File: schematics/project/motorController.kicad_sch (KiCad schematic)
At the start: 0 parts

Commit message: some progress, dust slowly clears
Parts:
- added Q1, Q2, Q3, Q4, Q5, Q6: BSS123, Package_TO_SOT_SMD:SOT-23, symbol Transistor_FET:BSS123
- added R10, R11, R12, R7, R8, R9: 1k, Resistor_SMD:R_0603_1608Metric, symbol Device:R
- added R4, R5, R6: R, Resistor_SMD:R_0603_1608Metric, symbol Device:R
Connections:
- net cruise: now also R10.2
- net hiPoBreak: now also R12.2
- net lowPoBreak: now also R11.2
- net reverse: now also R7.2
- net speed_fast: now also R8.2
- net speed_slow: now also R9.2
- new net: Q2.1 (G), R8.1
- new net: Q3.1 (G), R9.1
- new net: Q5.1 (G), R11.1
- new net: Q4.1 (G), R10.1
- new net: Q6.1 (G), R12.1
- new net: Q1.1 (G), R7.1
- new net +48V: Q6.3 (D)
- new net GND: R4.1, R5.1, R6.1
- new net GNDPWR: Q1.2 (S), Q2.2 (S), Q3.2 (S), Q4.2 (S), Q5.2 (S)
- new net Hall1: R4.2
- new net Hall2: R5.2
- new net Hall3: R6.2
- new net cruise_IN: Q4.3 (D)
- new net hiPoBreak_IN: Q6.2 (S)
- new net lowPoBreak_IN: Q5.3 (D)
- new net reverse_IN: Q1.3 (D), Q3.3 (D)
- new net speed_fast_IN: Q2.3 (D)
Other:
- removed sheet 3 Speed
- sheet Dig2Analog ports: added Analog, PWM; removed none

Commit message: small progress, angsthasen
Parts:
- R4, R5, R6: value R -> 1k
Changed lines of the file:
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@@
     (effects (font (size 1.27 1.27)) (justify left bottom))
   )
-  (label "throttle_IN" (at 110.49 40.64 0)
+  (label "throttle_a" (at 110.49 40.64 0)
     (effects (font (size 1.27 1.27)) (justify left bottom))
   )
@@
     (effects (font (size 1.27 1.27)) (justify right))
   )
-  (hierarchical_label "throttle_a" (shape input) (at 67.31 40.64 180)
+  (hierarchical_label "throttle_pwm" (shape input) (at 67.31 40.64 180)
     (effects (font (size 1.27 1.27)) (justify right))
   )
@@
       (effects (font (size 1.27 1.27)) (justify right))
     )
-    (property "Value" "R" (id 1) (at 215.9 149.8599 0)
+    (property "Value" "1k" (id 1) (at 215.9 149.8599 0)
       (effects (font (size 1.27 1.27)) (justify right))
     )
@@
       (effects (font (size 1.27 1.27)) (justify right))
     )
-    (property "Value" "R" (id 1) (at 231.14 149.8599 0)
+    (property "Value" "1k" (id 1) (at 231.14 149.8599 0)
       (effects (font (size 1.27 1.27)) (justify right))
     )
@@
       (effects (font (size 1.27 1.27)) (justify right))
     )
-    (property "Value" "R" (id 1) (at 223.52 149.8599 0)
-      (effects (font (size 1.27 1.27)) (justify right))
-    )
+    (property "Value" "1k" (id 1) (at 223.52 149.8599 0)
+      (effects (font (size 1.27 1.27)) (justify right))
+    )

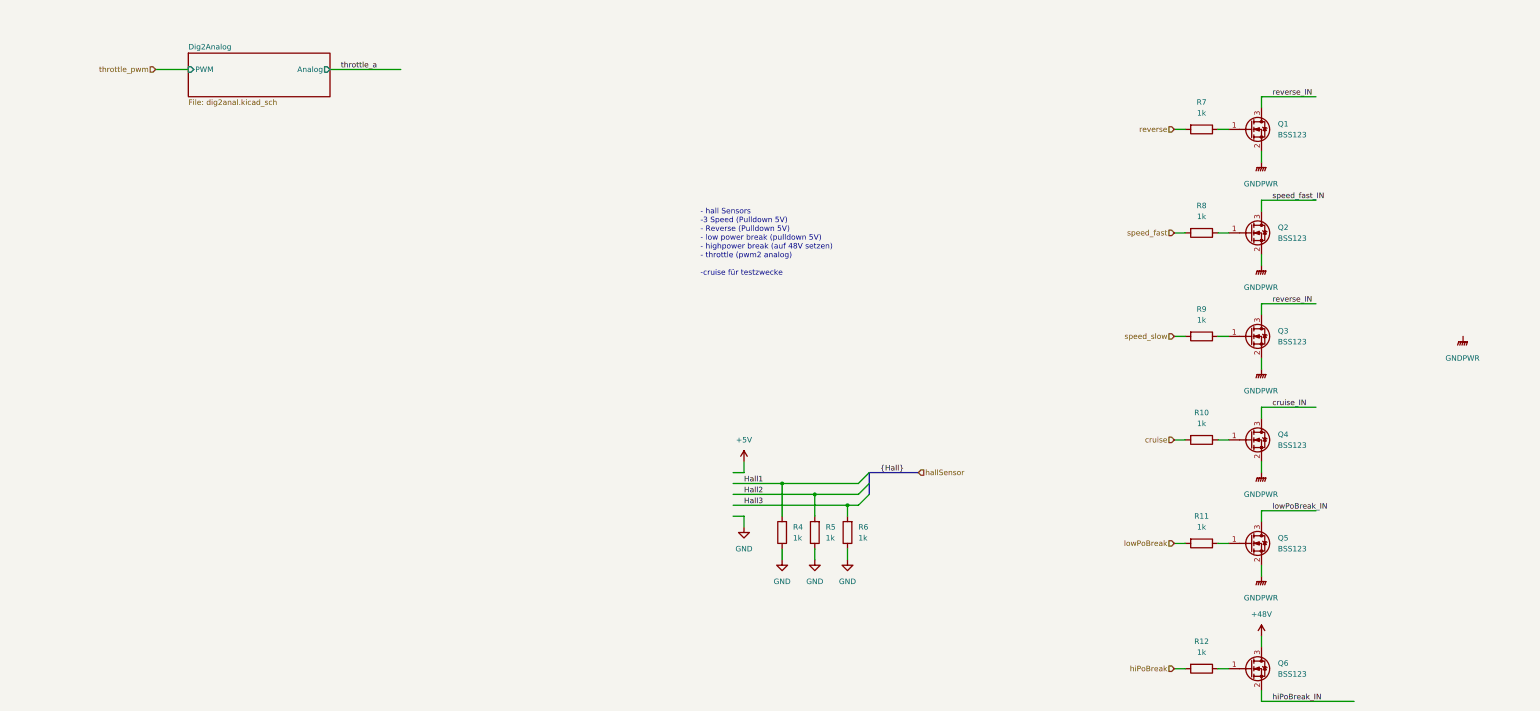
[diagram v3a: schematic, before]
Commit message: Adding separate library, BT Module
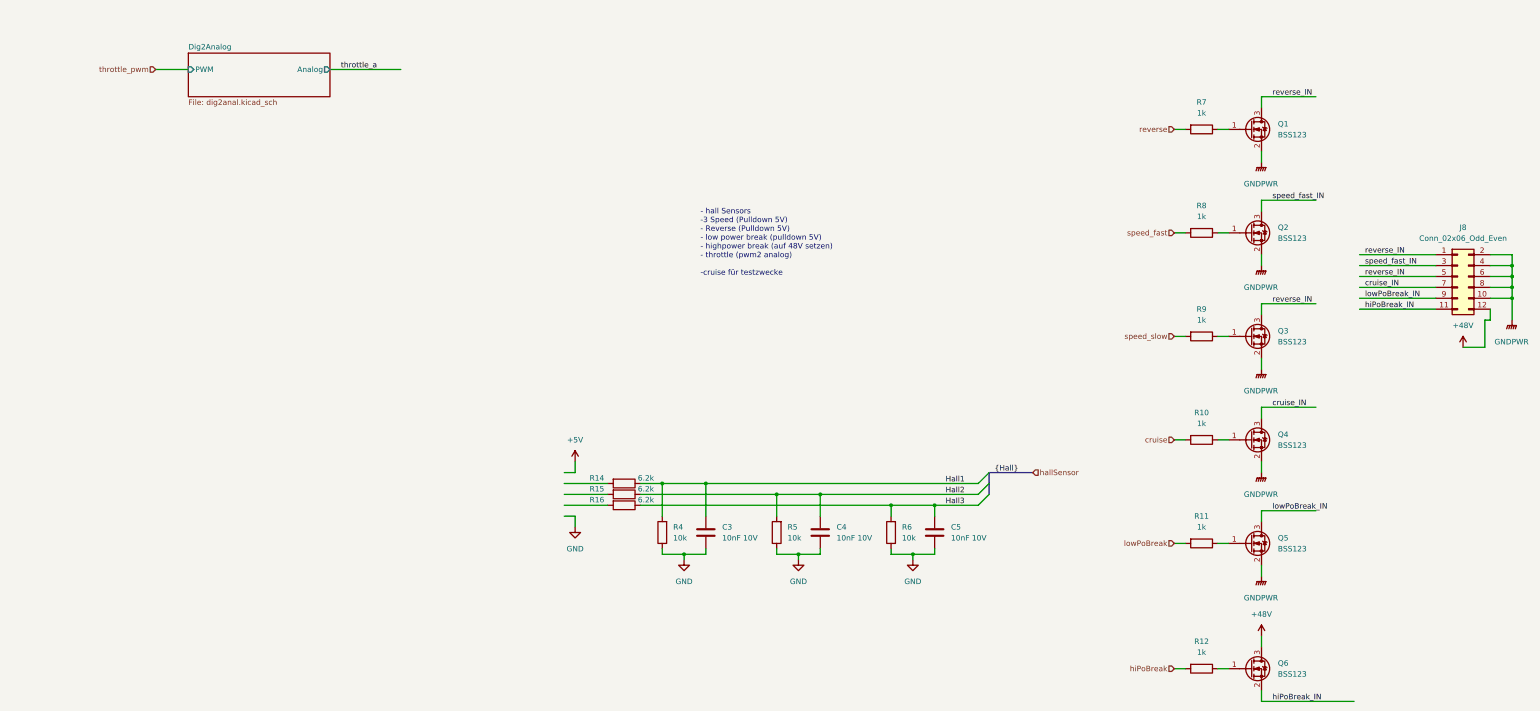
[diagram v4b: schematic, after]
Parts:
- added C3, C4, C5: 10nF 10V, Capacitor_SMD:C_0603_1608Metric, symbol Device:C
- added J8: Conn_02x06_Odd_Even, Connector_PinSocket_2.54mm:PinSocket_2x06_P2.54mm_Vertical_SMD, symbol Connector_Generic:Conn_02x06_Odd_Even
- added R14, R15, R16: 6.2k, Resistor_SMD:R_0603_1608Metric, symbol Device:R
- R4, R5, R6: value 1k -> 10k
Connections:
- net +48V: now also J8.12 (Pin_12)
- net GND: now also C3.2, C4.2, C5.2
- net GNDPWR: now also J8.10 (Pin_10), J8.2 (Pin_2), J8.4 (Pin_4), J8.6 (Pin_6), J8.8 (Pin_8)
- net Hall1: now also C3.1, R14.1
- net Hall2: now also C4.1, R15.1
- net Hall3: now also C5.1, R16.1
- net cruise_IN: now also J8.7 (Pin_7)
- net hiPoBreak_IN: now also J8.11 (Pin_11)
- net lowPoBreak_IN: now also J8.9 (Pin_9)
- net reverse_IN: now also J8.1 (Pin_1), J8.5 (Pin_5)
- net speed_fast_IN: now also J8.3 (Pin_3)
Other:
- moved on the sheet: R4, R5, R6

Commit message: random commit
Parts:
- added J10: Conn_01x05, Connector_JST:JST_SH_SM05B-SRSS-TB_1x05-1MP_P1.00mm_Horizontal, symbol Connector_Generic:Conn_01x05
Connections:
- net +5V: now also J10.5 (Pin_5)
- net GND: now also J10.1 (Pin_1)
- net reverse_IN: no longer J8.5 (Pin_5), Q3.3 (D)
- net at R16.2: now also J10.2 (Pin_2)
- net at R15.2: now also J10.3 (Pin_3)
- net at R14.2: now also J10.4 (Pin_4)
- new net speed_slow_IN: J8.5 (Pin_5), Q3.3 (D)
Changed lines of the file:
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@@
+    (effects (font (size 1.27 1.27)) (justify left bottom))
+  )
+  (label "speed_slow_IN" (at 349.25 88.9 0)
     (effects (font (size 1.27 1.27)) (justify left bottom))
   )
@@
     (effects (font (size 1.27 1.27)) (justify left bottom))
   )
-  (label "reverse_IN" (at 327.66 95.25 0)
-    (effects (font (size 1.27 1.27)) (justify left bottom))
-  )
-  (label "reverse_IN" (at 349.25 88.9 0)
+  (label "speed_slow_IN" (at 327.66 95.25 0)
     (effects (font (size 1.27 1.27)) (justify left bottom))
   )
@@
     (pin "3")
   )
+  (symbol (lib_id "Connector_Generic:Conn_01x05") (at 157.48 139.7 180) (unit 1)
+    (in_bom yes) (on_board yes) (fields_autoplaced)
+    (property "Reference" "J10" (id 0) (at 157.48 128.27 0))
+    (property "Value" "Conn_01x05" (id 1) (at 157.48 130.81 0))
+    (property "Footprint" "Connector_JST:JST_SH_SM05B-SRSS-TB_1x05-1MP_P1.00mm_Horizontal" (id 2) (at 157.48 139.7 0)
+      (effects (font (size 1.27 1.27)) hide)
+    )
+    (property "Datasheet" "~" (id 3) (at 157.48 139.7 0)
+      (effects (font (size 1.27 1.27)) hide)
+    )
+    (pin "1")
+    (pin "2")
+    (pin "3")
+    (pin "4")
+    (pin "5")
+  )
   (symbol (lib_id "power:+48V") (at 325.12 172.72 0) (unit 1)
     (in_bom yes) (on_board yes) (fields_autoplaced)
@@
   (symbol (lib_id "power:+48V") (at 372.11 105.41 0) (unit 1)
     (in_bom yes) (on_board yes) (fields_autoplaced)
-    (property "Reference" "#PWR?" (id 0) (at 372.11 109.22 0)
-      (effects (font (size 1.27 1.27)) hide)
-    )
+    (property "Reference" "#PWR0148" (id 0) (at 372.11 109.22 0)
+      (effects (font (size 1.27 1.27)) hide)
+    )
